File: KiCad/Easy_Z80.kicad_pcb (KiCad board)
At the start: 2 copper layers, 99.9 x 99.9 mm, 61 parts, among them J1 POWER, J2 SERIAL_A, J3 SERIAL_B, J4 VBAT, J5 RC2014_BUS, J6 RC2014_EXT, J7 RC2014_SPARE, SW1 RESET, U1 Z84C00, U10 74HCT670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

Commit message: PCB: Silkscreen fixes
Signed-off-by: Sergey Kiselev <skiselev@gmail.com>
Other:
- board text added: "Design files and documentation: github.com/skiselev/easy_z80"
- board text added: "Easy Z80 - Version 1.1 - Copyright (C) 2019 Max Malinov & Sergey Kiselev"
- board text removed: "Easy Z80 - Version 1.0 - Copyright (C) 2019 Max Malinov & Sergey Kiselev"

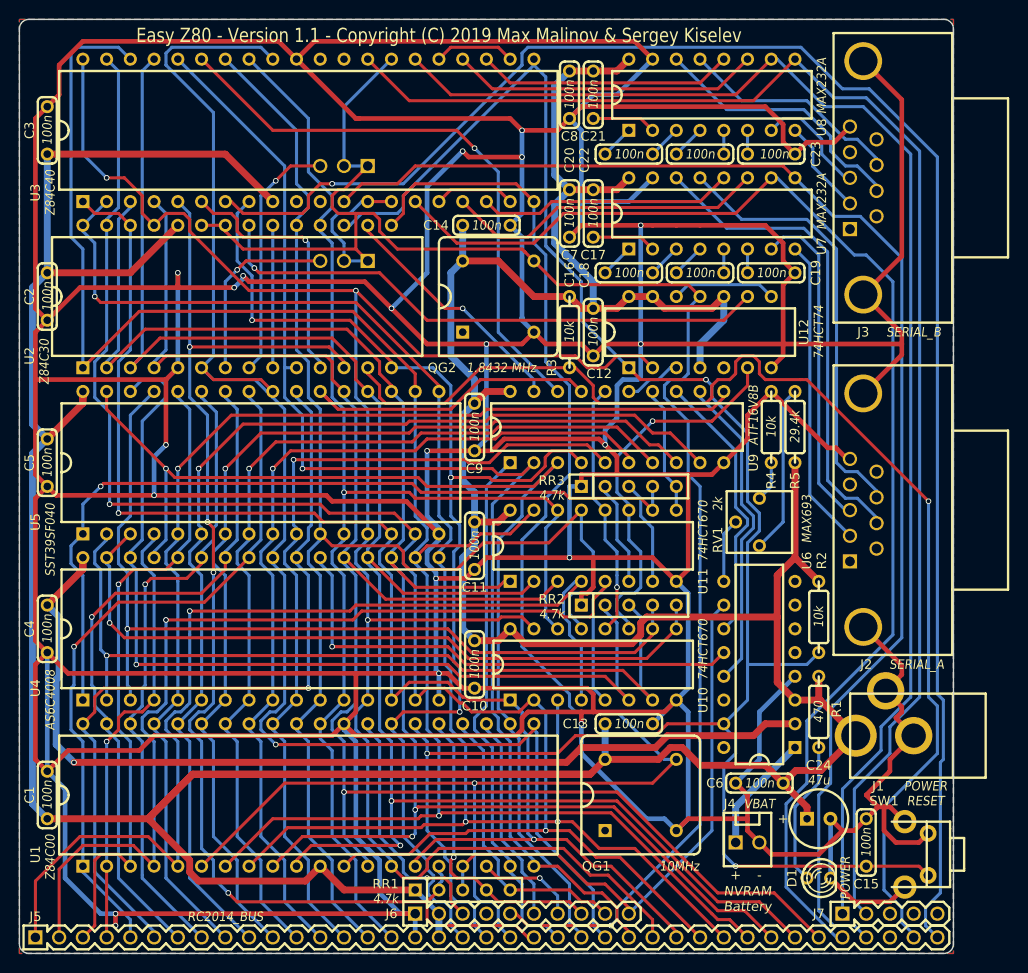
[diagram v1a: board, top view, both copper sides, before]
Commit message: KiCad: Replace files with version 1.1
Signed-off-by: Sergey Kiselev <skiselev@gmail.com>
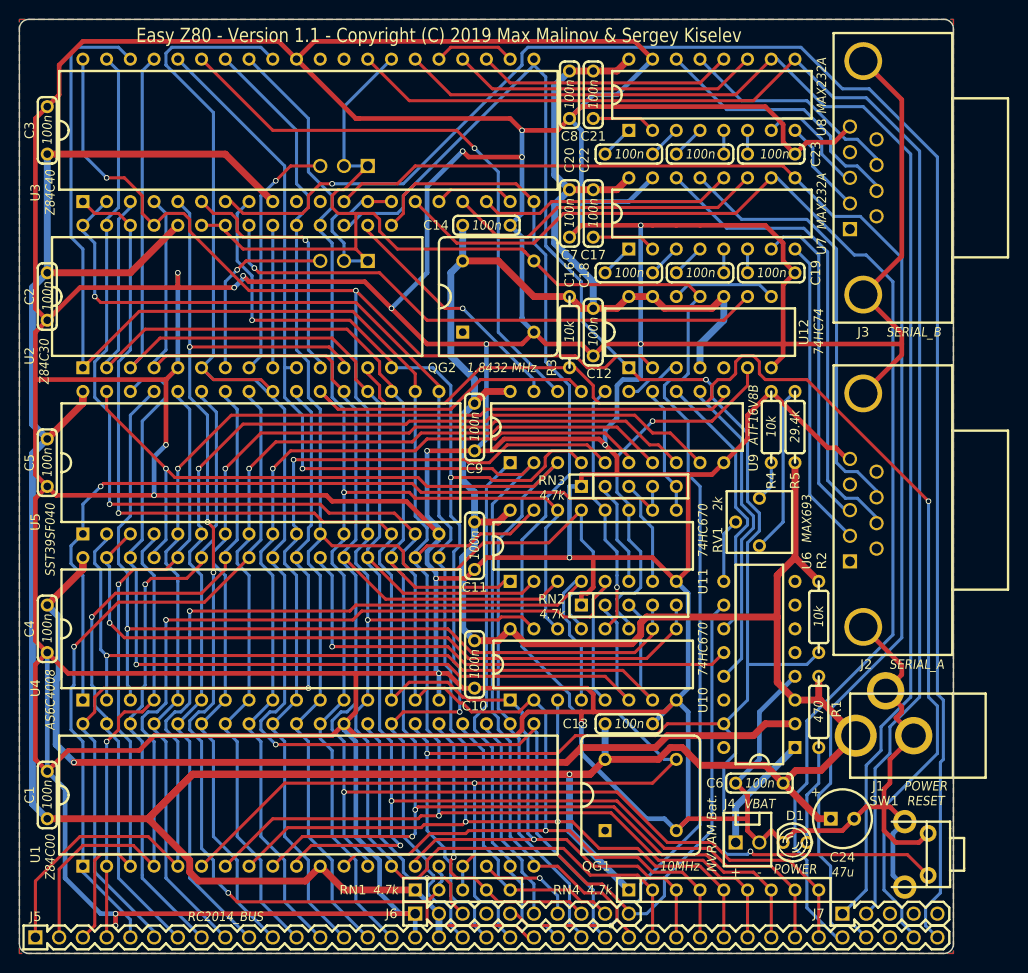
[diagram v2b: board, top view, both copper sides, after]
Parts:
- removed C15: 100n, My_Components:Cap_Cer_508
- added RN4: 4.7k, My_Components:Conn_SIL9, F.Cu at (152.4, 170.2)
- U10, U11: value 74HCT670 -> 74HC670
- U12: value 74HCT74 -> 74HC74
- moved D1 4.58 mm to (160.0, 165.1), turned to 180 degrees
- moved C24 2.54 mm to (165.1, 162.6)
- renumbered RR1 to RN1, RR2 to RN2, RR3 to RN3
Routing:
- net VCC: track 533.4 -> 550.3 mm, vias 0 -> 1
- net GND: track 1130.9 -> 1119.8 mm
- net Net-(D1-Pad2): track 15.5 -> 10.7 mm
- net /D1: track 153.7 -> 157.0 mm
- net /D3: track 174.2 -> 177.2 mm
- net /D7: track 180.5 -> 183.5 mm
- net /D6: track 197.5 -> 200.5 mm
- net /D5: track 180.3 -> 183.3 mm
- net /D2: track 176.4 -> 179.4 mm
- net /D4: track 210.1 -> 213.1 mm
- net /D0: track 205.9 -> 207.8 mm
- net /RXDB: track 151.8 -> 150.8 mm
- net /CH_A_CLK: track 191.5 -> 192.4 mm
- net /TXDA: track 138.2 -> 137.4 mm
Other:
- board text added: "NVRAM Bat."
